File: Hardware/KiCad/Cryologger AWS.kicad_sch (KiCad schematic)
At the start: 23 parts, among them J1 Screw_Terminal_01x02, J2 Screw_Terminal_01x04, J3 Screw_Terminal_01x04, J4 Screw_Terminal_01x04, U1 Adafruit_LSM303AGR, U10 Pololu_D36V6, U2 Adafruit_DPS310, U3 Adafruit_Feather_Header, U4 Adafruit_Feather_Header, U5 ROCKBLOCK_9603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

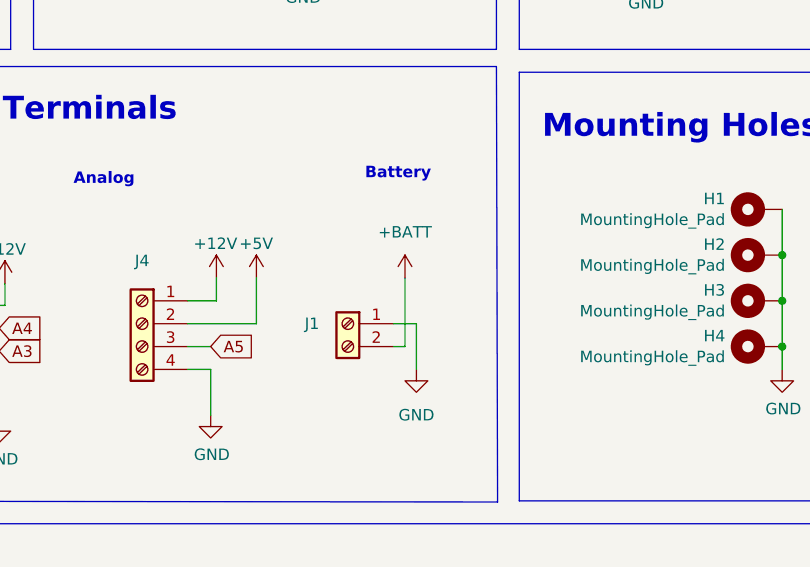
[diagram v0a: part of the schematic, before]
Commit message: Fix KiCad design error
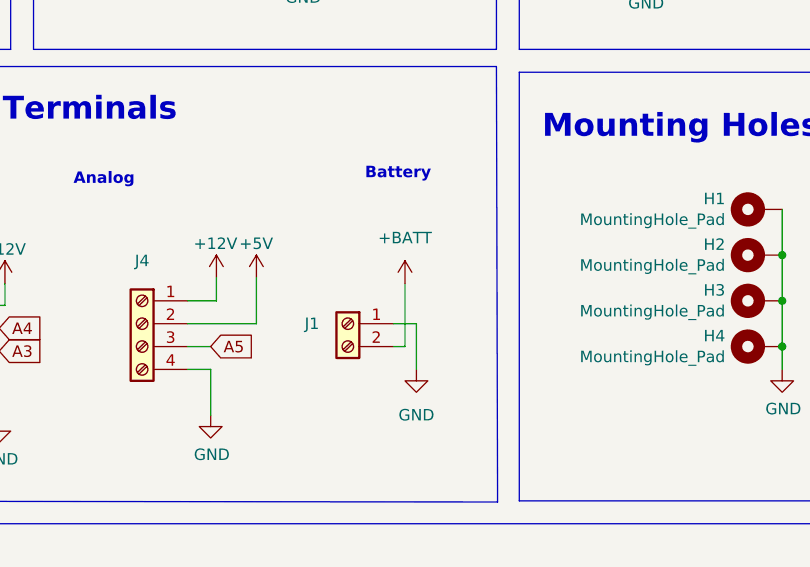
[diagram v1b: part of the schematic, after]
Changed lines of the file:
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@@
     (stroke (width 0) (type default) (color 0 0 0 0))
   )
-  (wire (pts (xy 235.585 95.25) (xy 235.585 87.63))
+  (wire (pts (xy 235.585 95.25) (xy 235.585 88.265))
     (stroke (width 0) (type default) (color 0 0 0 0))
   )
@@
     (pin "1")
   )
-  (symbol (lib_id "power:+BATT") (at 235.585 87.63 0) (unit 1)
+  (symbol (lib_id "power:+BATT") (at 235.585 88.265 0) (unit 1)
     (in_bom yes) (on_board yes) (fields_autoplaced)
-    (property "Reference" "#PWR015" (id 0) (at 235.585 91.44 0)
-      (effects (font (size 1.27 1.27)) hide)
-    )
-    (property "Value" "+BATT" (id 1) (at 235.585 82.55 0))
-    (property "Footprint" "" (id 2) (at 235.585 87.63 0)
-      (effects (font (size 1.27 1.27)) hide)
-    )
-    (property "Datasheet" "" (id 3) (at 235.585 87.63 0)
+    (property "Reference" "#PWR015" (id 0) (at 235.585 92.075 0)
+      (effects (font (size 1.27 1.27)) hide)
+    )
+    (property "Value" "+BATT" (id 1) (at 235.585 83.185 0))
+    (property "Footprint" "" (id 2) (at 235.585 88.265 0)
+      (effects (font (size 1.27 1.27)) hide)
+    )
+    (property "Datasheet" "" (id 3) (at 235.585 88.265 0)
       (effects (font (size 1.27 1.27)) hide)
     )
@@
   (symbol (lib_id "power:GND") (at 160.655 105.41 0) (unit 1)
     (in_bom yes) (on_board yes)
-    (property "Reference" "#PWR?" (id 0) (at 160.655 111.76 0)
+    (property "Reference" "#PWR0113" (id 0) (at 160.655 111.76 0)
       (effects (font (size 1.27 1.27)) hide)
     )
@@
   (symbol (lib_id "power:GND") (at 168.91 106.045 0) (unit 1)
     (in_bom yes) (on_board yes)
-    (property "Reference" "#PWR?" (id 0) (at 168.91 112.395 0)
+    (property "Reference" "#PWR0108" (id 0) (at 168.91 112.395 0)
       (effects (font (size 1.27 1.27)) hide)
     )
@@
       (reference "#PWR0107") (unit 1) (value "GND") (footprint "")
     )
+    (path "/fe839259-c60d-4b91-93e8-3532389c5946"
+      (reference "#PWR0108") (unit 1) (value "GND") (footprint "")
+    )
     (path "/38366ae1-7b05-4df4-b886-380218ad1cab"
       (reference "#PWR0109") (unit 1) (value "+12V") (footprint "")
@@
       (reference "#PWR0112") (unit 1) (value "+12V") (footprint "")
     )
+    (path "/6d8f1dc8-67a6-484e-bbfc-3427f989f5b4"
+      (reference "#PWR0113") (unit 1) (value "GND") (footprint "")
+    )
     (path "/46d61df5-6f9c-4adc-a561-3ee6eabf14c9"
       (reference "#PWR0114") (unit 1) (value "+12V") (footprint "")
@@
       (reference "#PWR0119") (unit 1) (value "+5V") (footprint "")
     )
-    (path "/6d8f1dc8-67a6-484e-bbfc-3427f989f5b4"
-      (reference "#PWR?") (unit 1) (value "GND") (footprint "")
-    )
-    (path "/fe839259-c60d-4b91-93e8-3532389c5946"
-      (reference "#PWR?") (unit 1) (value "GND") (footprint "")
-    )
     (path "/00000000-0000-0000-0000-00006081e600"
